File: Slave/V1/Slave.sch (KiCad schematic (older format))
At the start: 0 parts

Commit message: Routing signals
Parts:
- added J101, J102: 649002227222, Connectors:649002227222, symbol 649002227222
- added Q101: 2N7002P,215, IC:SOT-23-3, symbol 2N7002P,215
- added R101: RC0805JR-07470RL, Resistors:R0805, symbol RC0805JR-07470RL
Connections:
- new net: Q101.1 (G), R101.1
- new net DGND: Q101.2 (S)
- new net PWR_ENABLE: Q101.3 (D)
- new net PWR_ENABLE_GPIO: R101.2

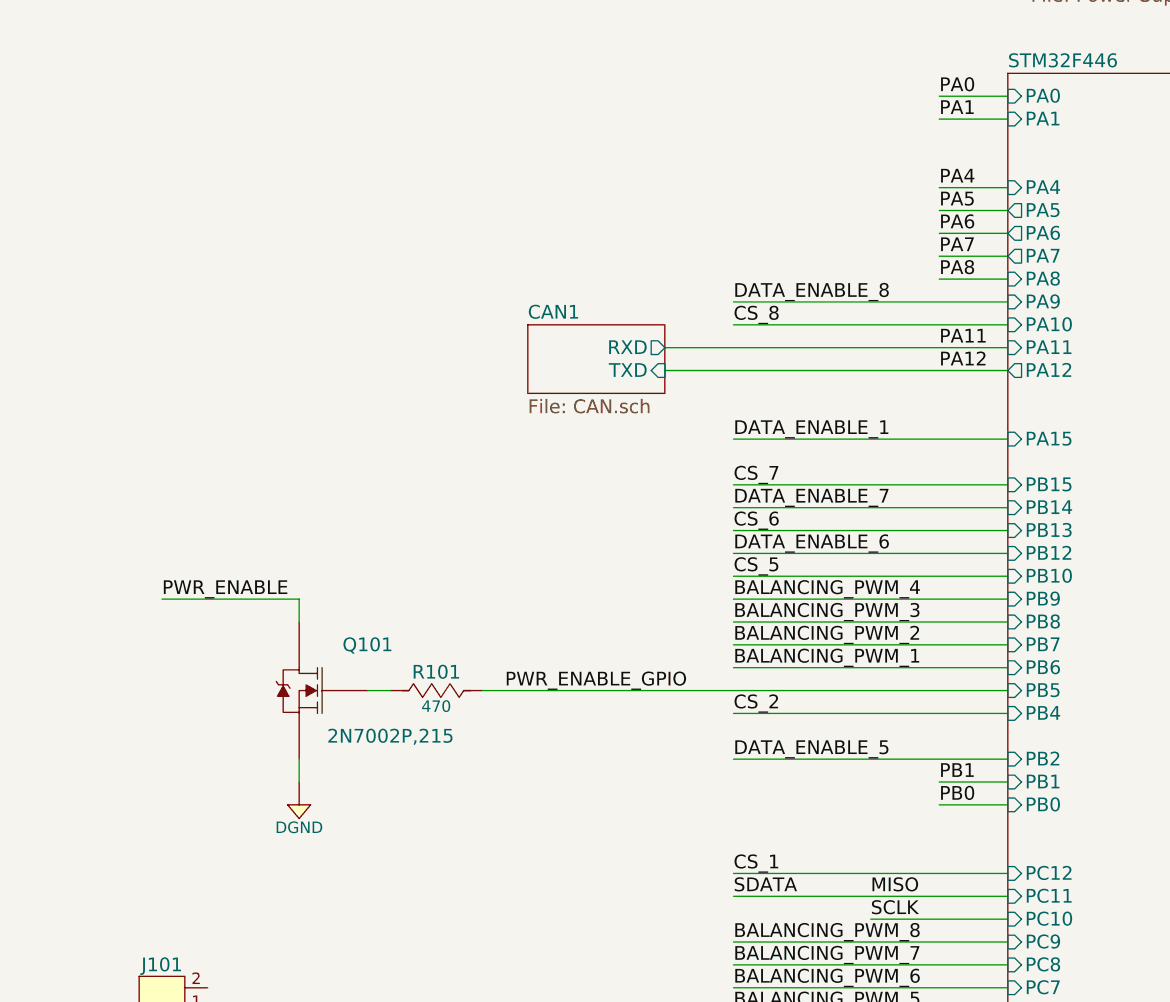
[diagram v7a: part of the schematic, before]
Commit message: Routing signals 2
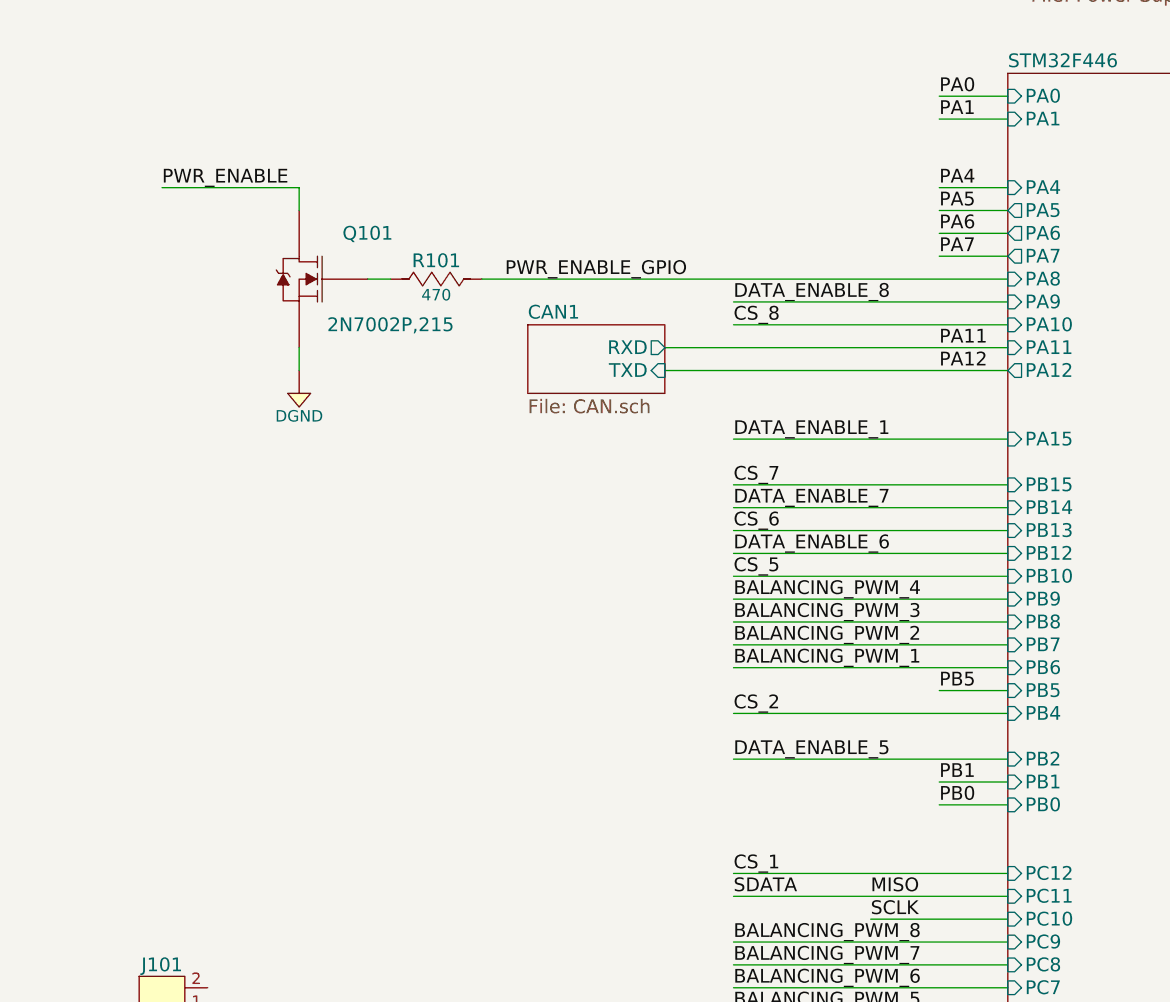
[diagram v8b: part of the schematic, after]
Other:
- moved on the sheet: Q101, R101
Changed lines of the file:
@@
 	8700 2100 9000 2100
-Wire Wire Line
-	8700 2200 9000 2200
 Wire Wire Line
 	7800 2300 9000 2300
@@
 L 2N7002P,215 Q101
 U 1 1 59465033
-P 6000 4000
-F 0 "Q101" H 5800 4200 60  0000 C CNN
-F 1 "2N7002P,215" H 5700 3800 60  0000 C CNN
-F 2 "IC:SOT-23-3" H 6150 3100 60  0001 C CNN
-F 3 "http://assets.nexperia.com/documents/data-sheet/2N7002P.pdf" H 6150 3000 60  0001 C CNN
-F 4 "Digikey" H 6150 3600 60  0001 C CNN "Supplier"
-F 5 "1727-4692-1-ND" H 6150 3500 60  0001 C CNN "Supplier Part Number"
-F 6 "Nexperia USA Inc." H 6150 3400 60  0001 C CNN "Manufacturer"
-F 7 "2N7002P,215" H 6100 3300 60  0001 C CNN "Manufacturer Part Number"
-F 8 "MOSFET N-CH 60V 0.36A SOT-23" H 6150 3200 60  0001 C CNN "Description"
-	1    6000 4000
+P 6000 2200
+F 0 "Q101" H 5800 2400 60  0000 C CNN
+F 1 "2N7002P,215" H 5700 2000 60  0000 C CNN
+F 2 "IC:SOT-23-3" H 6150 1300 60  0001 C CNN
+F 3 "http://assets.nexperia.com/documents/data-sheet/2N7002P.pdf" H 6150 1200 60  0001 C CNN
+F 4 "Digikey" H 6150 1800 60  0001 C CNN "Supplier"
+F 5 "1727-4692-1-ND" H 6150 1700 60  0001 C CNN "Supplier Part Number"
+F 6 "Nexperia USA Inc." H 6150 1600 60  0001 C CNN "Manufacturer"
+F 7 "2N7002P,215" H 6100 1500 60  0001 C CNN "Manufacturer Part Number"
+F 8 "MOSFET N-CH 60V 0.36A SOT-23" H 6150 1400 60  0001 C CNN "Description"
+	1    6000 2200
 	-1   0    0    -1
 $EndComp
@@
 L DGND #PWR017
 U 1 1 59465039
-P 5900 4500
-F 0 "#PWR017" H 5900 4330 50  0001 C CNN
-F 1 "DGND" H 5900 4400 50  0000 C CNN
-F 2 "" H 5900 4600 60  0000 C CNN
-F 3 "" H 5880 4410 60  0000 C CNN
-	1    5900 4500
-	1    0    0    -1
-$EndComp
-Wire Wire Line
-	5900 4300 5900 4400
-Text Label 5300 3600 0    60   ~ 0
-PWR_ENABLE
-Wire Wire Line
-	5300 3600 5900 3600
-Wire Wire Line
-	5900 3600 5900 3700
+P 5900 2700
+F 0 "#PWR017" H 5900 2530 50  0001 C CNN
+F 1 "DGND" H 5900 2600 50  0000 C CNN
+F 2 "" H 5900 2800 60  0000 C CNN
+F 3 "" H 5880 2610 60  0000 C CNN
+	1    5900 2700
+	1    0    0    -1
+$EndComp
+Wire Wire Line
+	5900 2500 5900 2600
+Text Label 5300 1800 0    60   ~ 0
+PWR_ENABLE
+Wire Wire Line
+	5300 1800 5900 1800
+Wire Wire Line
+	5900 1800 5900 1900
 $Comp
 L RC0805JR-07470RL R101
 U 1 1 59465190
-P 6500 4000
-F 0 "R101" H 6500 4080 60  0000 C CNN
-F 1 "RC0805JR-07470RL" H 6500 3700 50  0001 C CNN
-F 2 "Resistors:R0805" H 6500 3100 30  0001 C CNN
-F 3 "http://www.yageo.com/documents/recent/PYu-RC_Group_51_RoHS_L_7.pdf" H 6500 3050 30  0001 C CNN
-F 4 "Digikey" H 6500 3600 60  0001 C CNN "Supplier"
-F 5 "311-470ARCT-ND" H 6500 3500 60  0001 C CNN "Supplier Part Number"
-F 6 "Yageo" H 6500 3400 60  0001 C CNN "Manufacturer"
-F 7 "RC0805JR-07470RL" H 6500 3300 60  0001 C CNN "Manufacturer Part Number"
-F 8 "RES SMD 470 OHM 5% 1/8W 0805" H 6500 3200 60  0001 C CNN "Description"
-F 9 "470" H 6500 3930 50  0000 C CNN "Resistance (Ohms)"
-F 10 "±5%" H 6910 3920 50  0001 C CNN "Tolerance (%)"
-F 11 "1/8W" H 6500 3860 50  0001 C CNN "Puissance (Watts)"
-	1    6500 4000
-	1    0    0    -1
-$EndComp
-Wire Wire Line
-	6200 4000 6300 4000
+P 6500 2200
+F 0 "R101" H 6500 2280 60  0000 C CNN
+F 1 "RC0805JR-07470RL" H 6500 1900 50  0001 C CNN
+F 2 "Resistors:R0805" H 6500 1300 30  0001 C CNN
+F 3 "http://www.yageo.com/documents/recent/PYu-RC_Group_51_RoHS_L_7.pdf" H 6500 1250 30  0001 C CNN
+F 4 "Digikey" H 6500 1800 60  0001 C CNN "Supplier"
+F 5 "311-470ARCT-ND" H 6500 1700 60  0001 C CNN "Supplier Part Number"
+F 6 "Yageo" H 6500 1600 60  0001 C CNN "Manufacturer"
+F 7 "RC0805JR-07470RL" H 6500 1500 60  0001 C CNN "Manufacturer Part Number"
+F 8 "RES SMD 470 OHM 5% 1/8W 0805" H 6500 1400 60  0001 C CNN "Description"
+F 9 "470" H 6500 2130 50  0000 C CNN "Resistance (Ohms)"
+F 10 "±5%" H 6910 2120 50  0001 C CNN "Tolerance (%)"
+F 11 "1/8W" H 6500 2060 50  0001 C CNN "Puissance (Watts)"
+	1    6500 2200
+	1    0    0    -1
+$EndComp
+Wire Wire Line
+	6200 2200 6300 2200
 Text Label 7800 4900 0    60   ~ 0
 SDATA
@@
 Text Label 7800 5300 0    60   ~ 0
 BALANCING_PWM_6
-Text Label 6800 4000 0    60   ~ 0
+Text Label 6800 2200 0    60   ~ 0
 PWR_ENABLE_GPIO
 Wire Wire Line
-	6700 4000 9000 4000
+	6700 2200 9000 2200
 Text Label 7800 4800 0    60   ~ 0
 CS_1
@@
 Text Label 7800 2400 0    60   ~ 0
 CS_8
-Text Label 8700 2200 0    60   ~ 0
-PA8
 $Comp
 L 649002227222 J101
@@
 	1    0    0    -1
 $EndComp
+Text Label 8700 4000 0    60   ~ 0
+PB5
+Wire Wire Line
+	8700 4000 9000 4000
 $EndSCHEMATC
